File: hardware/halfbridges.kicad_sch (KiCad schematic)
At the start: 7 parts

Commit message: update L6226Q footprint and symbol
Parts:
- U?: footprint easyeda2kicad:VQFN-32_L5.0-W5.0-P0.50-TL-EP -> matei:ST-L6226Q-VQFN32
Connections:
- net GND: no longer U?.10 (NC), U?.18 (NC), U?.32 (NC)
- new net: U?.10 (NC), U?.18 (NC), U?.32 (NC)
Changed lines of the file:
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@@
       (effects (font (size 1.27 1.27)))
     )
-    (property "Footprint" "easyeda2kicad:VQFN-32_L5.0-W5.0-P0.50-TL-EP" (at 137.16 129.54 0)
+    (property "Footprint" "matei:ST-L6226Q-VQFN32" (at 137.16 129.54 0)
       (effects (font (size 1.27 1.27)) hide)
     )

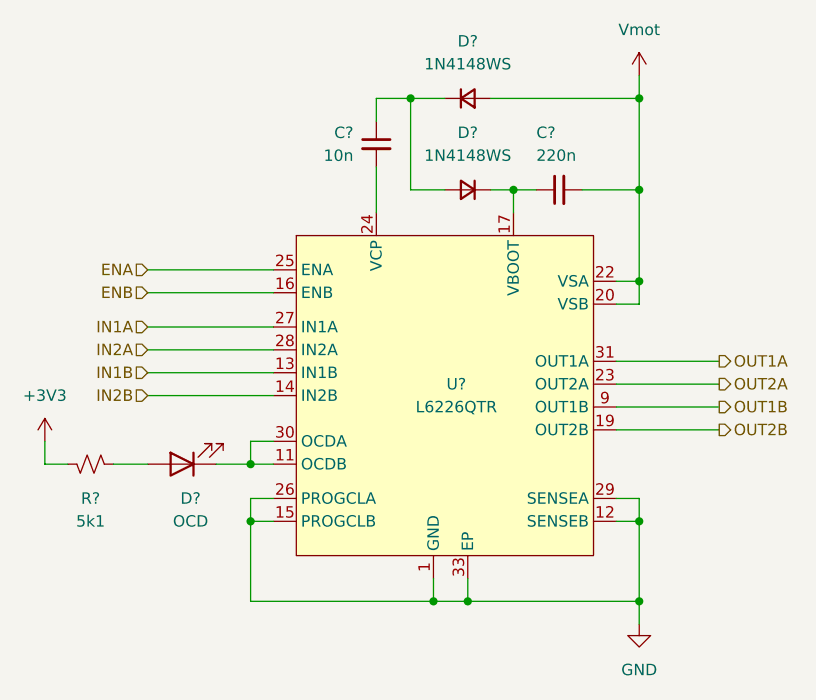
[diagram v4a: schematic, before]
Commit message: Update firmware defines to match hardware
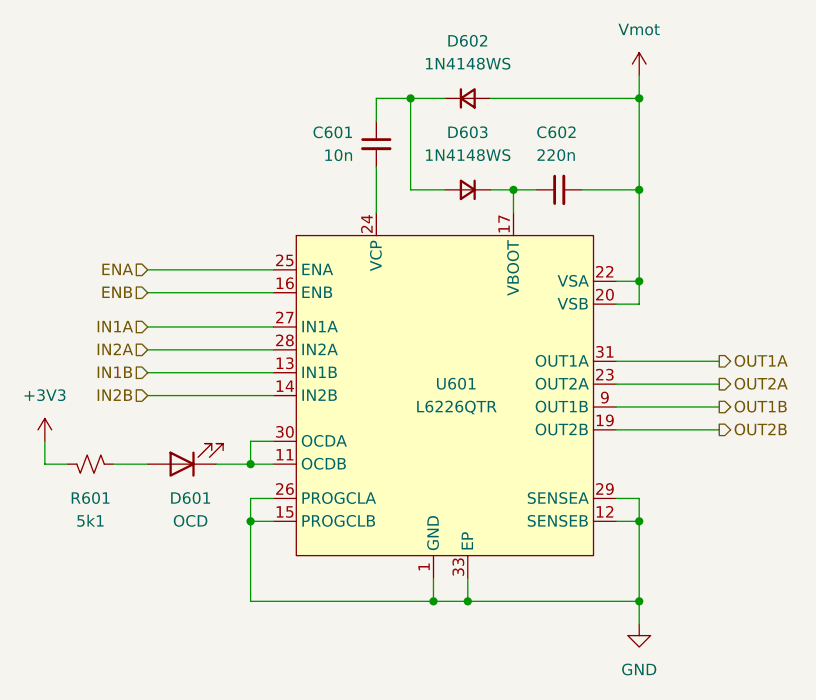
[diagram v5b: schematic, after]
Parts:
- gave numbers to parts that had none: 7
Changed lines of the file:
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@@
   (symbol (lib_id "easyeda2kicad:L6226QTR") (at 137.16 91.44 0) (unit 1)
     (in_bom yes) (on_board yes) (dnp no)
-    (property "Reference" "U?" (at 138.43 90.17 0)
+    (property "Reference" "U601" (at 138.43 90.17 0)
       (effects (font (size 1.27 1.27)))
     )
@@
     (instances
       (project "lemon-pepper"
-        (path "/0306e2fa-4433-4288-91d9-65a3484207ad"
-          (reference "U?") (unit 1)
-        )
         (path "/0306e2fa-4433-4288-91d9-65a3484207ad/ac193888-c8ba-43d9-af32-3c2e2d16ba47"
           (reference "U601") (unit 1)
@@
   (symbol (lib_id "matei:Vmot") (at 158.75 55.88 0) (unit 1)
     (in_bom yes) (on_board yes) (dnp no) (fields_autoplaced)
-    (property "Reference" "#PWR0105" (at 153.67 59.69 0)
+    (property "Reference" "#PWR0602" (at 153.67 59.69 0)
       (effects (font (size 1.27 1.27)) hide)
     )
@@
     (instances
       (project "lemon-pepper"
-        (path "/0306e2fa-4433-4288-91d9-65a3484207ad"
-          (reference "#PWR0105") (unit 1)
-        )
         (path "/0306e2fa-4433-4288-91d9-65a3484207ad/ac193888-c8ba-43d9-af32-3c2e2d16ba47"
           (reference "#PWR0602") (unit 1)
@@
   (symbol (lib_id "power:GND") (at 158.75 116.84 0) (unit 1)
     (in_bom yes) (on_board yes) (dnp no) (fields_autoplaced)
-    (property "Reference" "#PWR0103" (at 158.75 123.19 0)
+    (property "Reference" "#PWR0603" (at 158.75 123.19 0)
       (effects (font (size 1.27 1.27)) hide)
     )
@@
     (instances
       (project "lemon-pepper"
-        (path "/0306e2fa-4433-4288-91d9-65a3484207ad"
-          (reference "#PWR0103") (unit 1)
-        )
         (path "/0306e2fa-4433-4288-91d9-65a3484207ad/ac193888-c8ba-43d9-af32-3c2e2d16ba47"
           (reference "#PWR0603") (unit 1)
@@
   (symbol (lib_id "Device:R_Small_US") (at 97.79 99.06 270) (mirror x) (unit 1)
     (in_bom yes) (on_board yes) (dnp no)
-    (property "Reference" "R?" (at 97.79 102.87 90)
+    (property "Reference" "R601" (at 97.79 102.87 90)
       (effects (font (size 1.27 1.27)))
     )
@@
     (instances
       (project "lemon-pepper"
-        (path "/0306e2fa-4433-4288-91d9-65a3484207ad"
-          (reference "R?") (unit 1)
-        )
         (path "/0306e2fa-4433-4288-91d9-65a3484207ad/ac193888-c8ba-43d9-af32-3c2e2d16ba47"
           (reference "R601") (unit 1)
@@
   (symbol (lib_id "Device:D_Small") (at 139.7 58.42 0) (unit 1)
     (in_bom yes) (on_board yes) (dnp no) (fields_autoplaced)
-    (property "Reference" "D?" (at 139.7 52.07 0)
+    (property "Reference" "D602" (at 139.7 52.07 0)
       (effects (font (size 1.27 1.27)))
     )
@@
     (instances
       (project "lemon-pepper"
-        (path "/0306e2fa-4433-4288-91d9-65a3484207ad"
-          (reference "D?") (unit 1)
-        )
         (path "/0306e2fa-4433-4288-91d9-65a3484207ad/ac193888-c8ba-43d9-af32-3c2e2d16ba47"
           (reference "D602") (unit 1)
@@
   (symbol (lib_id "Device:C_Small") (at 149.86 68.58 90) (mirror x) (unit 1)
     (in_bom yes) (on_board yes) (dnp no)
-    (property "Reference" "C?" (at 147.32 62.23 90)
+    (property "Reference" "C602" (at 147.32 62.23 90)
       (effects (font (size 1.27 1.27)) (justify right))
     )
@@
     (instances
       (project "lemon-pepper"
-        (path "/0306e2fa-4433-4288-91d9-65a3484207ad"
-          (reference "C?") (unit 1)
-        )
         (path "/0306e2fa-4433-4288-91d9-65a3484207ad/ac193888-c8ba-43d9-af32-3c2e2d16ba47"
           (reference "C602") (unit 1)
@@
   (symbol (lib_id "Device:C_Small") (at 129.54 63.5 0) (unit 1)
     (in_bom yes) (on_board yes) (dnp no)
-    (property "Reference" "C?" (at 127 62.2363 0)
+    (property "Reference" "C601" (at 127 62.2363 0)
       (effects (font (size 1.27 1.27)) (justify right))
     )
@@
     (instances
       (project "lemon-pepper"
-        (path "/0306e2fa-4433-4288-91d9-65a3484207ad"
-          (reference "C?") (unit 1)
-        )
         (path "/0306e2fa-4433-4288-91d9-65a3484207ad/ac193888-c8ba-43d9-af32-3c2e2d16ba47"
           (reference "C601") (unit 1)
@@
   (symbol (lib_id "Device:D_Small") (at 139.7 68.58 0) (mirror y) (unit 1)
     (in_bom yes) (on_board yes) (dnp no)
-    (property "Reference" "D?" (at 139.7 62.23 0)
+    (property "Reference" "D603" (at 139.7 62.23 0)
       (effects (font (size 1.27 1.27)))
     )
@@
     (instances
       (project "lemon-pepper"
-        (path "/0306e2fa-4433-4288-91d9-65a3484207ad"
-          (reference "D?") (unit 1)
-        )
         (path "/0306e2fa-4433-4288-91d9-65a3484207ad/ac193888-c8ba-43d9-af32-3c2e2d16ba47"
           (reference "D603") (unit 1)
@@
   (symbol (lib_id "power:+3V3") (at 92.71 96.52 0) (unit 1)
     (in_bom yes) (on_board yes) (dnp no) (fields_autoplaced)
-    (property "Reference" "#PWR0109" (at 92.71 100.33 0)
+    (property "Reference" "#PWR0601" (at 92.71 100.33 0)
       (effects (font (size 1.27 1.27)) hide)
     )
@@
     (instances
       (project "lemon-pepper"
-        (path "/0306e2fa-4433-4288-91d9-65a3484207ad"
-          (reference "#PWR0109") (unit 1)
-        )
         (path "/0306e2fa-4433-4288-91d9-65a3484207ad/ac193888-c8ba-43d9-af32-3c2e2d16ba47"
           (reference "#PWR0601") (unit 1)
@@
   (symbol (lib_id "Device:LED") (at 107.95 99.06 180) (unit 1)
     (in_bom yes) (on_board yes) (dnp no)
-    (property "Reference" "D?" (at 108.9025 102.87 0)
+    (property "Reference" "D601" (at 108.9025 102.87 0)
       (effects (font (size 1.27 1.27)))
     )
@@
     (instances
       (project "lemon-pepper"
-        (path "/0306e2fa-4433-4288-91d9-65a3484207ad"
-          (reference "D?") (unit 1)
-        )
         (path "/0306e2fa-4433-4288-91d9-65a3484207ad/ac193888-c8ba-43d9-af32-3c2e2d16ba47"
           (reference "D601") (unit 1)

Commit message: Update BOM field LCSC ID
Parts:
- C601: LCSC ID (none) -> C15195; LCSC Part C15195 -> (none)
- C602: LCSC ID (none) -> C16772; LCSC Part C16772 -> (none)
- D601: LCSC ID (none) -> C2286; LCSC Part C2286 -> (none)
- D602, D603: LCSC ID (none) -> C2128; LCSC Part C2128 -> (none)
- R601: LCSC ID (none) -> C25905; LCSC Part C25905 -> (none)
- U601: LCSC ID (none) -> C95357; LCSC Part C95357 -> (none)
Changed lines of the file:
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@@
 			)
 		)
-		(property "LCSC Part" "C95357"
-			(at 137.16 134.62 0)
+		(property "LCSC ID" "C95357"
+			(at 137.16 91.44 0)
 			(effects
 				(font
@@
 			)
 		)
-		(property "LCSC Part" "C25905"
+		(property "LCSC ID" "C25905"
 			(at 97.79 99.06 0)
 			(effects
@@
 			)
 		)
-		(property "LCSC Part" "C2128"
+		(property "LCSC ID" "C2128"
 			(at 139.7 58.42 0)
 			(effects
@@
 			)
 		)
-		(property "LCSC Part" "C16772"
+		(property "LCSC ID" "C16772"
 			(at 149.86 68.58 0)
 			(effects
@@
 			)
 		)
-		(property "LCSC Part" "C15195"
+		(property "LCSC ID" "C15195"
 			(at 129.54 63.5 0)
 			(effects
@@
 			)
 		)
-		(property "LCSC Part" "C2128"
+		(property "LCSC ID" "C2128"
 			(at 139.7 68.58 0)
 			(effects
@@
 			)
 		)
-		(property "LCSC Part" "C2286"
+		(property "LCSC ID" "C2286"
 			(at 107.95 99.06 0)
 			(effects
